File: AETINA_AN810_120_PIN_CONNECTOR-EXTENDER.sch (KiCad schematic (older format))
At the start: 4 parts, among them J1 QTH-060-01-X-D-A, J2 QSH-060-01-X-D-A

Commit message: Routing completed
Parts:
- added unit 2 of J1
- added unit 2 of J2
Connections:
- net labels added: AVDD_TS_DIS, BRIDGE_EN, BRIDGE_IRQ, CHARGER_PRSNT, DP0_AUX_CH_N, DP0_AUX_CH_P, DP0_TX0_N, DP0_TX0_P, DP0_TX1_N, DP0_TX1_P, DP0_TX2_N, DP0_TX2_P, DP0_TX3_N, DP0_TX3_P, DP_HPD, DSI0_CLK_N, DSI0_CLK_P, DSI0_D0_N, DSI0_D0_P, DSI0_D1_N, DSI0_D1_P, DSI1_CLK_N, DSI1_CLK_P, DSI1_D0_N, DSI1_D0_P, DSI1_D1_N, DSI1_D1_P, DSI2_CLK_N, DSI2_CLK_P, DSI2_D0_N, DSI2_D0_P, DSI2_D1_N, DSI2_D1_P, DSI3_CLK_N, DSI3_CLK_P, DSI3_D0_N, DSI3_D0_P, DSI3_D1_N, DSI3_D1_P, GND, GSYNC_HSYNC, GSYNC_VSYNC, I2C_GP0_CLK, I2C_GP0_DAT, I2C_GP1_CLK, I2C_GP1_DAT, LCD_BIAS_EN, LCD_BKLT0_PWM, LCD_BKLT1_PWM, LCD_BKLT_EN, LCD_EN, LCD_TE, LCD_VDD_EN, NVSR_INT, SPI2_CS0, SPI2_MISO, SPI2_MOSI, SPI2_SCK, VDD_1V2, VDD_1V8, VDD_3V3_SLP, VDD_3V3_SYS, VDD_5V0_IO_SYS, VDD_DIS_3V3_LCD, VDD_LCD_1V8_DIS, VDD_SYS_BL, VDD_TS_1V8
- wire segments 0 -> 251
- no-connect marks 0 -> 35
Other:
- moved on the sheet: H1, H2, J1A, J2A

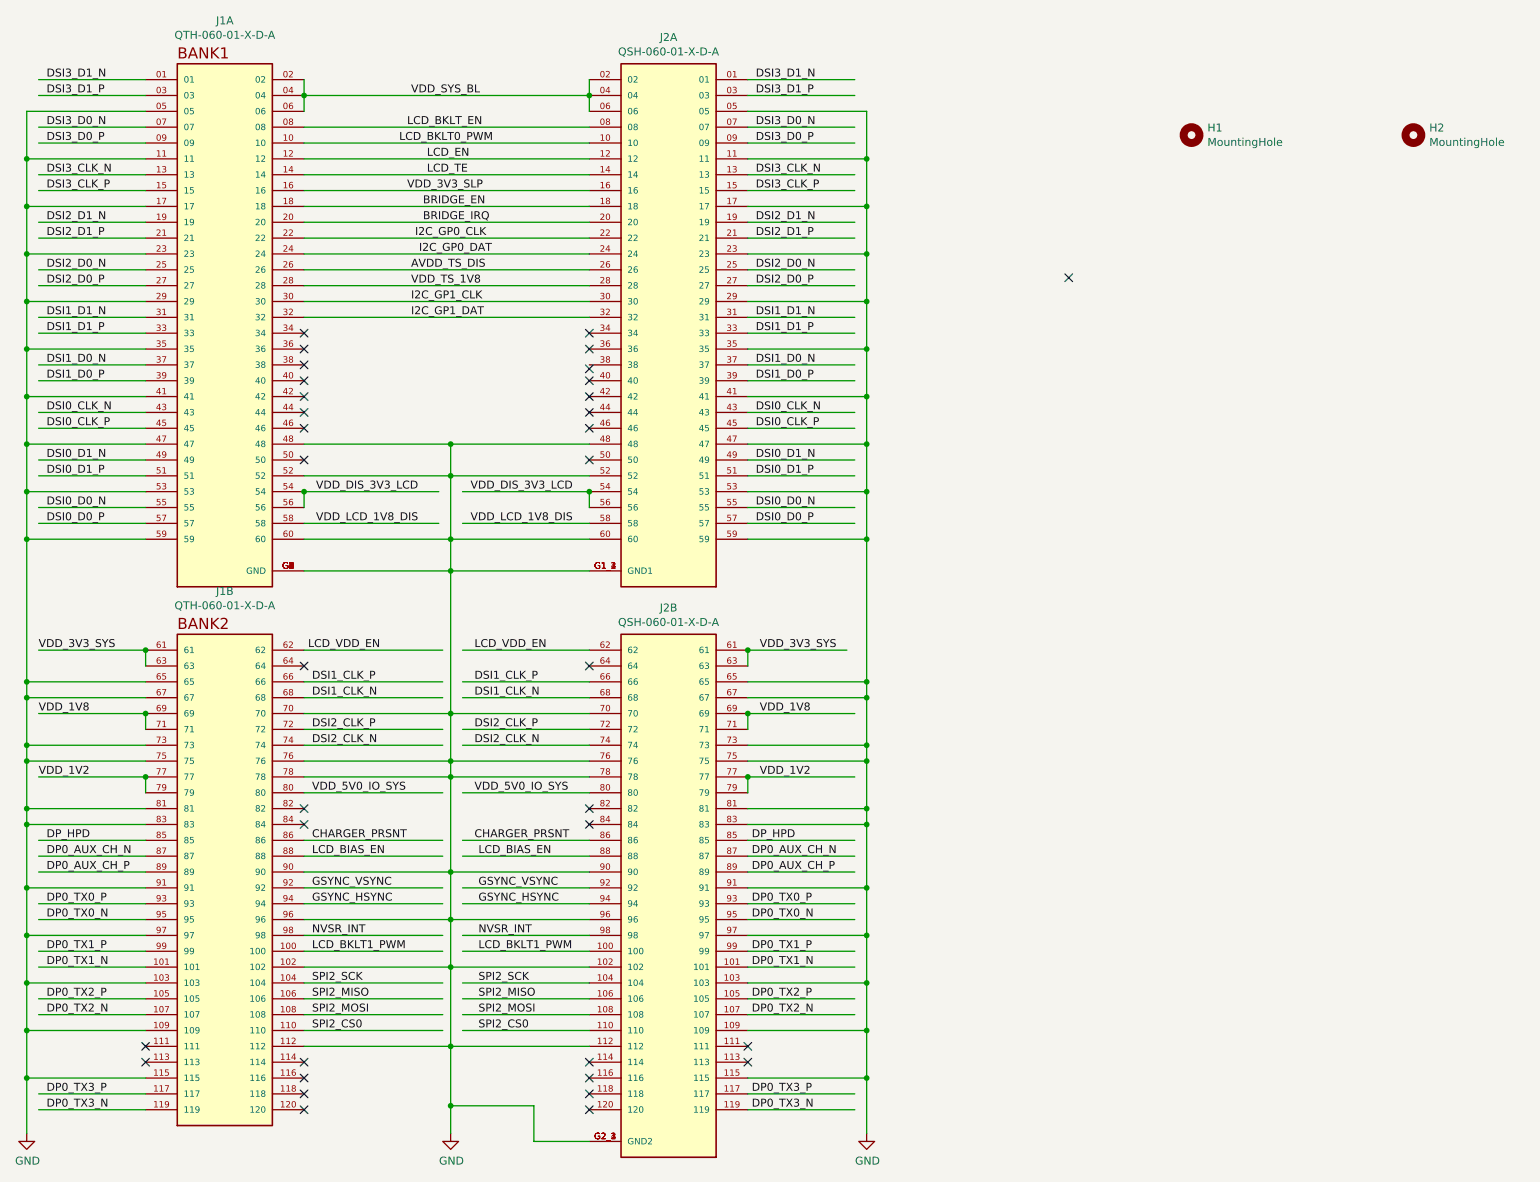
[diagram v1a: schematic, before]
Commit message: Fix wrong wiring by referring to incorrect connector
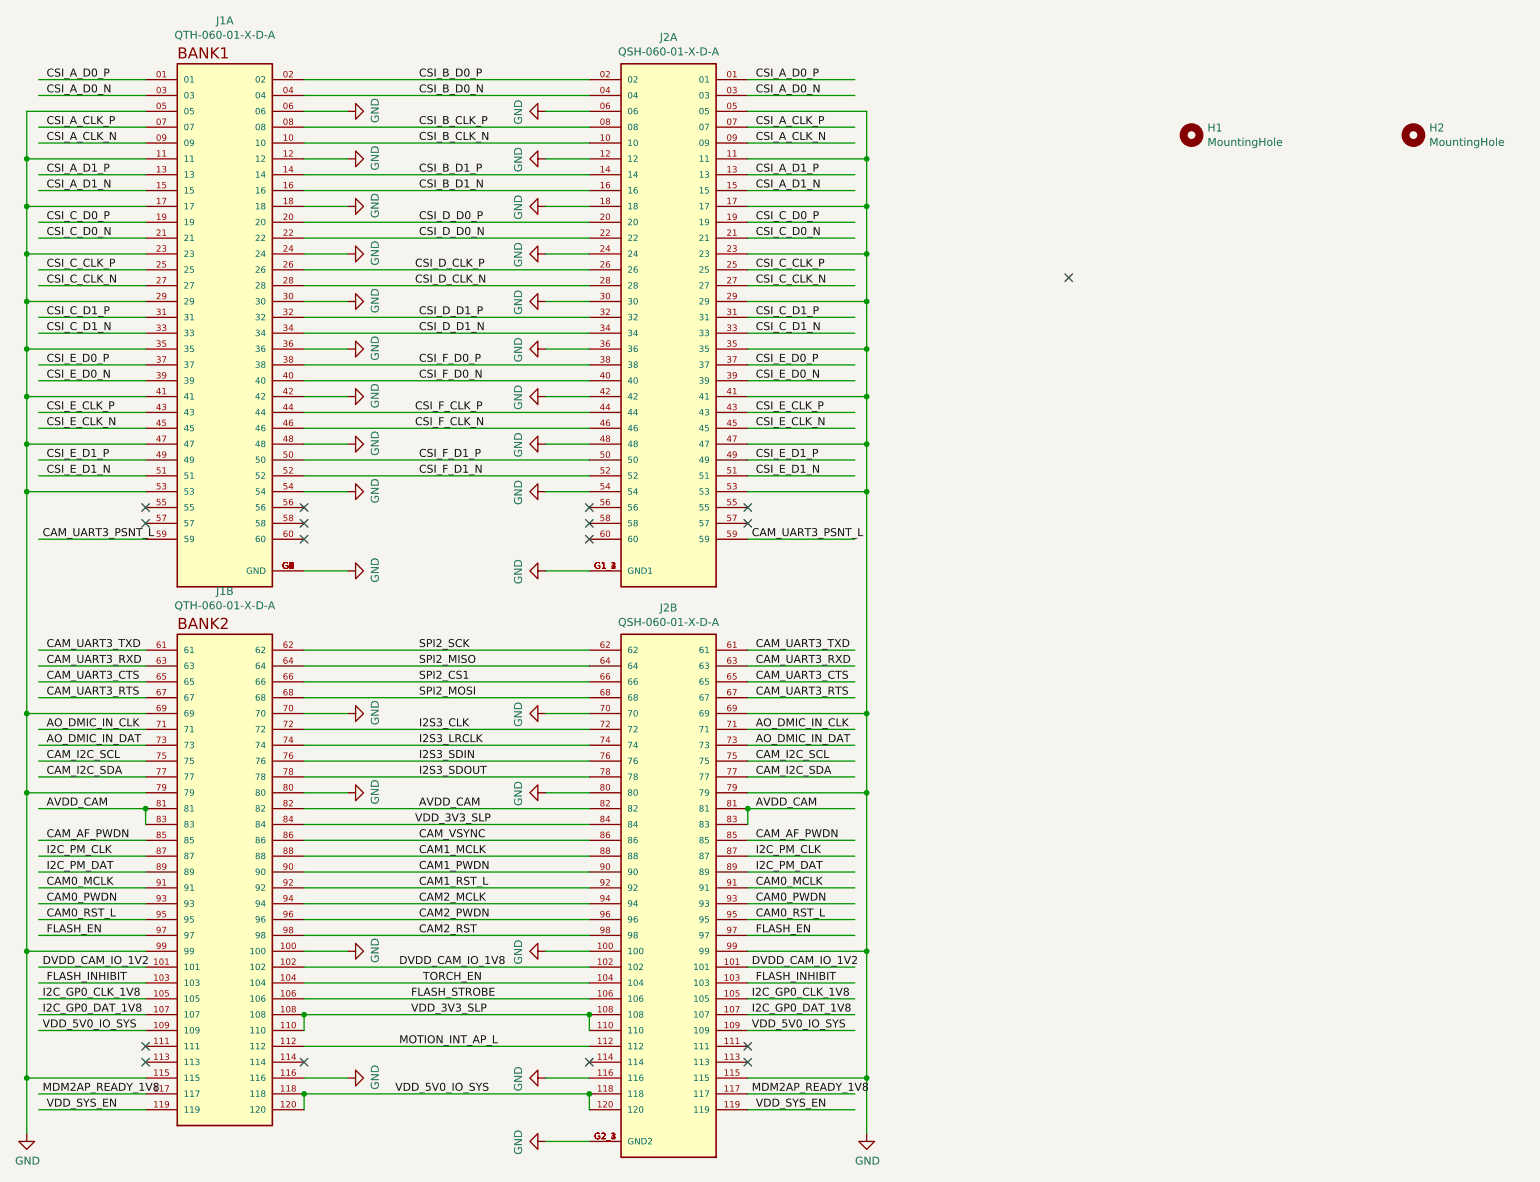
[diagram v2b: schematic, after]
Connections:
- net labels added: AO_DMIC_IN_CLK, AO_DMIC_IN_DAT, AVDD_CAM, CAM0_MCLK, CAM0_PWDN, CAM0_RST_L, CAM1_MCLK, CAM1_PWDN, CAM1_RST_L, CAM2_MCLK, CAM2_PWDN, CAM2_RST, CAM_AF_PWDN, CAM_I2C_SCL, CAM_I2C_SDA, CAM_UART3_CTS, CAM_UART3_PSNT_L, CAM_UART3_RTS, CAM_UART3_RXD, CAM_UART3_TXD, CAM_VSYNC, CSI_A_CLK_N, CSI_A_CLK_P, CSI_A_D0_N, CSI_A_D0_P, CSI_A_D1_N, CSI_A_D1_P, CSI_B_CLK_N, CSI_B_CLK_P, CSI_B_D0_N, CSI_B_D0_P, CSI_B_D1_N, CSI_B_D1_P, CSI_C_CLK_N, CSI_C_CLK_P, CSI_C_D0_N, CSI_C_D0_P, CSI_C_D1_N, CSI_C_D1_P, CSI_D_CLK_N, CSI_D_CLK_P, CSI_D_D0_N, CSI_D_D0_P, CSI_D_D1_N, CSI_D_D1_P, CSI_E_CLK_N, CSI_E_CLK_P, CSI_E_D0_N, CSI_E_D0_P, CSI_E_D1_N, CSI_E_D1_P, CSI_F_CLK_N, CSI_F_CLK_P, CSI_F_D0_N, CSI_F_D0_P, CSI_F_D1_N, CSI_F_D1_P, DVDD_CAM_IO_1V2, DVDD_CAM_IO_1V8, FLASH_EN, FLASH_INHIBIT, FLASH_STROBE, I2C_GP0_CLK_1V8, I2C_GP0_DAT_1V8, I2C_PM_CLK, I2C_PM_DAT, I2S3_CLK, I2S3_LRCLK, I2S3_SDIN, I2S3_SDOUT, MDM2AP_READY_1V8, MOTION_INT_AP_L, SPI2_CS1, TORCH_EN, VDD_SYS_EN
- net labels removed: AVDD_TS_DIS, BRIDGE_EN, BRIDGE_IRQ, CHARGER_PRSNT, DP0_AUX_CH_N, DP0_AUX_CH_P, DP0_TX0_N, DP0_TX0_P, DP0_TX1_N, DP0_TX1_P, DP0_TX2_N, DP0_TX2_P, DP0_TX3_N, DP0_TX3_P, DP_HPD, DSI0_CLK_N, DSI0_CLK_P, DSI0_D0_N, DSI0_D0_P, DSI0_D1_N, DSI0_D1_P, DSI1_CLK_N, DSI1_CLK_P, DSI1_D0_N, DSI1_D0_P, DSI1_D1_N, DSI1_D1_P, DSI2_CLK_N, DSI2_CLK_P, DSI2_D0_N, DSI2_D0_P, DSI2_D1_N, DSI2_D1_P, DSI3_CLK_N, DSI3_CLK_P, DSI3_D0_N, DSI3_D0_P, DSI3_D1_N, DSI3_D1_P, GSYNC_HSYNC, GSYNC_VSYNC, I2C_GP0_CLK, I2C_GP0_DAT, I2C_GP1_CLK, I2C_GP1_DAT, LCD_BIAS_EN, LCD_BKLT0_PWM, LCD_BKLT1_PWM, LCD_BKLT_EN, LCD_EN, LCD_TE, LCD_VDD_EN, NVSR_INT, SPI2_CS0, VDD_1V2, VDD_1V8, VDD_3V3_SYS, VDD_DIS_3V3_LCD, VDD_LCD_1V8_DIS, VDD_SYS_BL, VDD_TS_1V8
- wire segments 251 -> 212
- no-connect marks 35 -> 17
